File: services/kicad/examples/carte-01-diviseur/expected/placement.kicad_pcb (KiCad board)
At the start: 2 copper layers, 20 x 14 mm, 5 parts, among them J1 IN

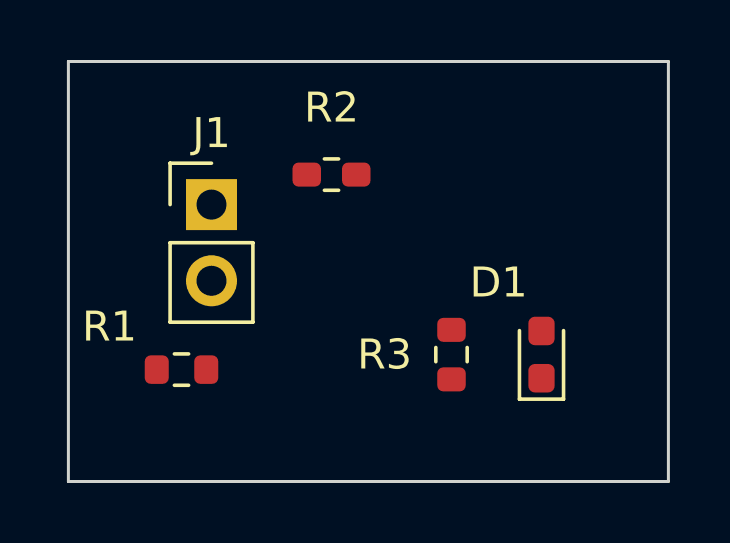
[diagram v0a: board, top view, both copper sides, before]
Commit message: feat(placement): les peripheriques se REPARTISSENT, ils ne s empilent plus
Question de l utilisateur devant le rendu : « c est quoi ce type de placement ? ».
Les composants s entassaient d un seul cote du boitier, etiquettes de
serigraphie l une sur l autre, trois quarts de la couronne vides.

TROIS CAUSES, toutes dans `_poser_les_peripheriques`, toutes la meme faute —
un angle unique pour tout un groupe :

  - les DIRECTS qui visent la meme broche (tous les decouplages d un rail,
    toutes les resistances d un meme signal) recevaient le MEME `angle_vers`
    et le meme rayon de depart ;
  - les SUIVEURS d un meme parent recevaient tous atan2(parent - centre) ;
  - les ISOLES partaient tous de l angle 0.0, c est-a-dire du meme point.

`le_long_du_rayon` ne s ecartait qu une fois la place prise : d ou la file.

REMEDE : `_ecart_en_eventail`. Le PREMIER de chaque groupe garde EXACTEMENT la
direction calculee — c est la topologie, on ne la perd pas pour faire joli — et
les suivants s ecartent symetriquement de 3 x `_PAS_ANGLE_DEG`.
Rien de deja pose ne bouge : seul l ANGLE DE DEPART de la recherche change, et
`le_long_du_rayon` reste seul juge de ce qui est libre.

BANC DES DIX CARTES, contour resserre ET peripheriques repartis :

    carte             demandee    livree         err  manq
    carte-01           25 x 20    20,1 x 13,6     0    0
    carte-02           55 x 40    34,9 x 25,2     0    0
    carte-03           50 x 35    27,6 x 19,9     0    0
    carte-04           60 x 45    36,6 x 29,8     0    0
    carte-05           70 x 50    40,0 x 32,6     0    0
    carte-06           80 x 60    46,5 x 36,4     0    0
    carte-07          110 x 80    47,7 x 38,8     0    0
    carte-08          125 x 95    57,4 x 44,1     0    0
    carte-09          130 x 100   57,8 x 45,2     0    0
    carte-10          140 x 105   59,0 x 45,8     0    0

Dix sur dix, 100 % route. carte-07 gagne 5,5 mm de largeur sur le passage
precedent, carte-06 deux, carte-10 deux. Sur ca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
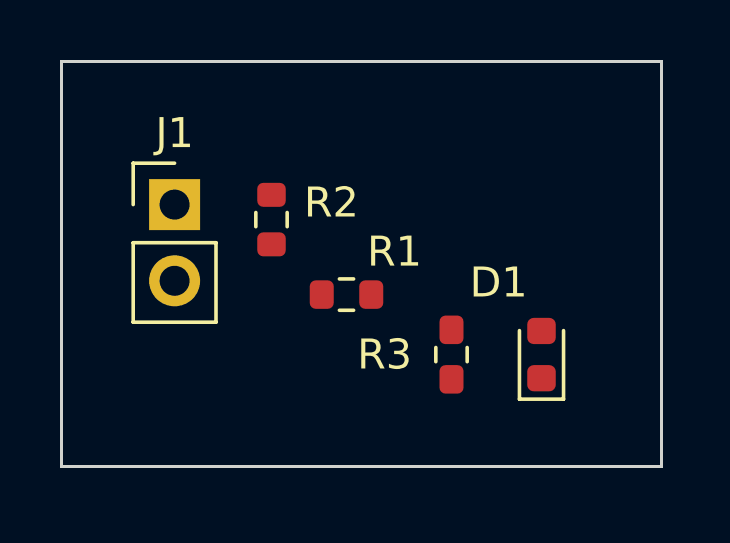
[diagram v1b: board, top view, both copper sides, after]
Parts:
- moved R1 6.04 mm to (145.5, 103.0)
- moved R2 2.50 mm to (143.0, 100.5), turned to 270 degrees
- moved J1 1.23 mm to (139.8, 100.0)
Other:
- board size 20 x 14 mm -> 20 x 13.5 mm
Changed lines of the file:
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@@
 (kicad_pcb
-	(version 20260206)
+	(version 20241229)
 	(generator "kicad_tools")
 	(generator_version "10.0")
@@
 	(title_block
 		(title "Cirqix PCB")
-		(date "2026-09-13")
+		(date "2026-09-23")
 		(rev 1.0)
 		(company "")
@@
 		(generator "kicad-footprint-generator")
 		(layer "F.Cu")
-		(at 141 100 0)
+		(at 139.77 100 0)
 		(descr "Through hole straight pin header, 1x02, 2.54mm pitch, single row")
 		(tags "Through hole pin header THT 1x02 2.54mm single row")
@@
 		(generator "kicad-footprint-generator")
 		(layer "F.Cu")
-		(at 140 105.5 0)
+		(at 145.5 103 0)
 		(descr "Resistor SMD 0603 (1608 Metric), square (rectangular) end terminal, IPC-7351 nominal, (Body size source: IPC-SM-782 page 72, https://www.pcb-3d.com/wordpress/wp-content/uploads/ipc-sm-782a_amendment_1_and_2.pdf)")
 		(tags "resistor")
 		(property "Reference" "R1"
-			(at -2.4 -1.43 0)
+			(at 1.6 -1.43 0)
 			(layer "F.SilkS")
 			(effects
@@
 		(generator "kicad-footprint-generator")
 		(layer "F.Cu")
-		(at 145 99 0)
+		(at 143 100.5 270)
 		(descr "Resistor SMD 0603 (1608 Metric), square (rectangular) end terminal, IPC-7351 nominal, (Body size source: IPC-SM-782 page 72, https://www.pcb-3d.com/wordpress/wp-content/uploads/ipc-sm-782a_amendment_1_and_2.pdf)")
 		(tags "resistor")
 		(property "Reference" "R2"
-			(at -1.46958e-16 -2.23 0)
+			(at -0.565685 -1.99569 0)
 			(layer "F.SilkS")
 			(effects
@@
 		)
 		(pad "1" smd roundrect
-			(at -0.825 0 90)
+			(at -0.825 0)
 			(size 0.8 0.95)
 			(layers "F.Cu" "F.Mask" "F.Paste")
@@
 		)
 		(pad "2" smd roundrect
-			(at 0.825 0 90)
+			(at 0.825 0)
 			(size 0.8 0.95)
 			(layers "F.Cu" "F.Mask" "F.Paste")
@@
 		)
 		(pad "1" smd roundrect
-			(at -0.7875 0 180)
+			(at -0.7875 0 270)
 			(size 0.875 0.95)
 			(layers "F.Cu" "F.Mask" "F.Paste")
@@
 		)
 		(pad "2" smd roundrect
-			(at 0.7875 0 180)
+			(at 0.7875 0 270)
 			(size 0.875 0.95)
 			(layers "F.Cu" "F.Mask" "F.Paste")
@@
 	)
 	(gr_rect
-		(start 136.230 95.230)
-		(end 156.230 109.230)
+		(start 136.000 95.230)
+		(end 156.000 108.730)
 		(stroke
 			(width 0.1)

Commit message: docs(banc): les dix boards du banc du 2026-09-23, service corrige
Artefacts du banc dont le tableau est deja commite : les dix cartes a
100 % route, 0 erreur, 0 connexion manquante, chacune a la taille de son
circuit.

Co-Authored-By: Claude Opus 5 <noreply@anthropic.com>
Claude-Session: https://claude.ai/code/session_01TnMqm4La2CxQHHB5K8aSSV
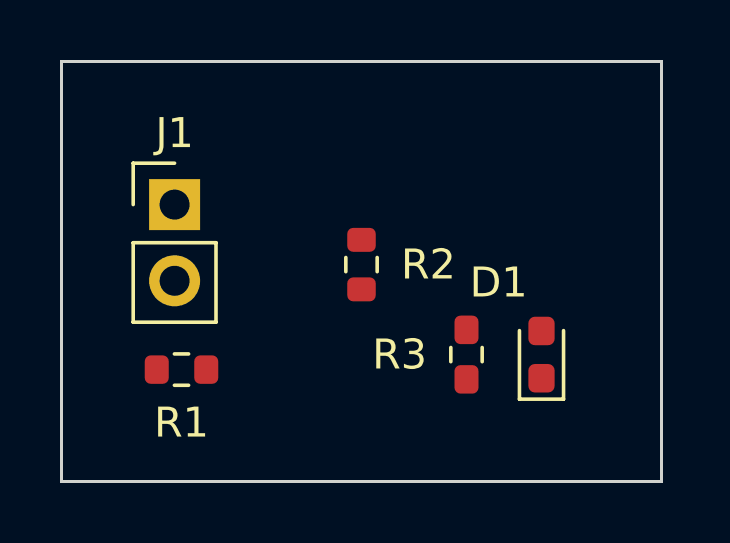
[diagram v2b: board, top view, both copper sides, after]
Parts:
- moved R1 6.04 mm to (140.0, 105.5)
- moved R2 3.35 mm to (146.0, 102.0)
- moved R3 0.50 mm to (149.5, 105.0)
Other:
- board size 20 x 13.5 mm -> 20 x 14 mm
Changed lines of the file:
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@@
 		(generator "kicad-footprint-generator")
 		(layer "F.Cu")
-		(at 145.5 103 0)
+		(at 140 105.5 0)
 		(descr "Resistor SMD 0603 (1608 Metric), square (rectangular) end terminal, IPC-7351 nominal, (Body size source: IPC-SM-782 page 72, https://www.pcb-3d.com/wordpress/wp-content/uploads/ipc-sm-782a_amendment_1_and_2.pdf)")
 		(tags "resistor")
 		(property "Reference" "R1"
-			(at 1.6 -1.43 0)
+			(at 1.95943e-16 1.77 0)
 			(layer "F.SilkS")
 			(effects
@@
 		(generator "kicad-footprint-generator")
 		(layer "F.Cu")
-		(at 143 100.5 270)
+		(at 146 102 270)
 		(descr "Resistor SMD 0603 (1608 Metric), square (rectangular) end terminal, IPC-7351 nominal, (Body size source: IPC-SM-782 page 72, https://www.pcb-3d.com/wordpress/wp-content/uploads/ipc-sm-782a_amendment_1_and_2.pdf)")
 		(tags "resistor")
 		(property "Reference" "R2"
-			(at -0.565685 -1.99569 0)
+			(at -1.46958e-16 -2.23 0)
 			(layer "F.SilkS")
 			(effects
@@
 		(generator "kicad-footprint-generator")
 		(layer "F.Cu")
-		(at 149 105 90)
+		(at 149.5 105 90)
 		(descr "Resistor SMD 0603 (1608 Metric), square (rectangular) end terminal, IPC-7351 nominal, (Body size source: IPC-SM-782 page 72, https://www.pcb-3d.com/wordpress/wp-content/uploads/ipc-sm-782a_amendment_1_and_2.pdf)")
 		(tags "resistor")
@@
 		)
 		(pad "1" smd roundrect
-			(at -0.7875 0 270)
+			(at -0.7875 0)
 			(size 0.875 0.95)
 			(layers "F.Cu" "F.Mask" "F.Paste")
@@
 		)
 		(pad "2" smd roundrect
-			(at 0.7875 0 270)
+			(at 0.7875 0)
 			(size 0.875 0.95)
 			(layers "F.Cu" "F.Mask" "F.Paste")
@@
 	(gr_rect
 		(start 136.000 95.230)
-		(end 156.000 108.730)
+		(end 156.000 109.230)
 		(stroke
 			(width 0.1)
